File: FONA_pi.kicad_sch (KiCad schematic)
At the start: 31 parts, among them J1 Conn_01x20_Socket, J10 Conn_01x04_Pin, J11 Conn_01x20_Socket, J12 Conn_01x20_Socket, J13 Conn_01x06_Socket, J14 Conn_01x06_Socket, J15 Conn_01x06_Socket, J16 Conn_01x06_Socket, J17 Conn_01x06_Socket, J18 Conn_01x04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

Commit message: Placed footprints again.
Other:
- moved on the sheet: D2, D3

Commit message: Fixed DRC errors
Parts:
- renumbered JP1 to G5
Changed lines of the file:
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@@
   (symbol (lib_id "Jumper:Jumper_2_Bridged") (at 135.89 95.25 180) (unit 1)
     (in_bom yes) (on_board yes) (dnp no)
-    (property "Reference" "JP1" (at 135.89 92.71 0)
+    (property "Reference" "G5" (at 135.89 92.71 0)
       (effects (font (size 1.27 1.27)))
     )
@@
       (project "FONA_pi"
         (path "/78cf560b-fde9-4d4c-9c9c-e6052c5bcb78"
-          (reference "JP1") (unit 1)
+          (reference "G5") (unit 1)
         )
       )

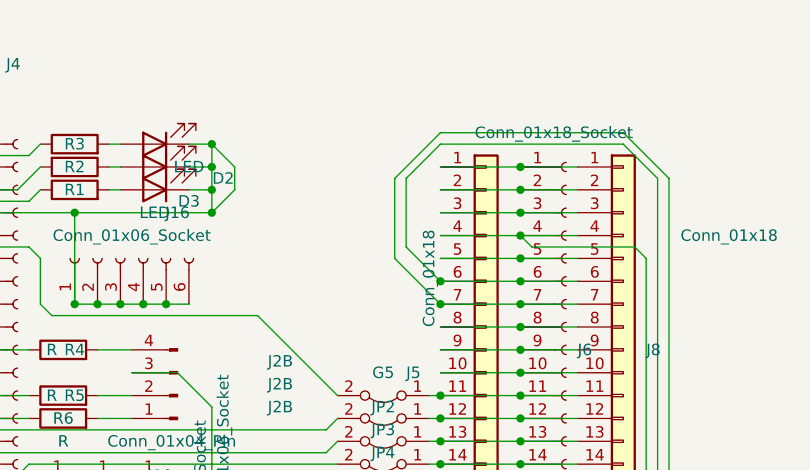
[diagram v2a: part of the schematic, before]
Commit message: Added connector pins J19 and J20, to associate with connectors in pcb.  Lost mounting holes
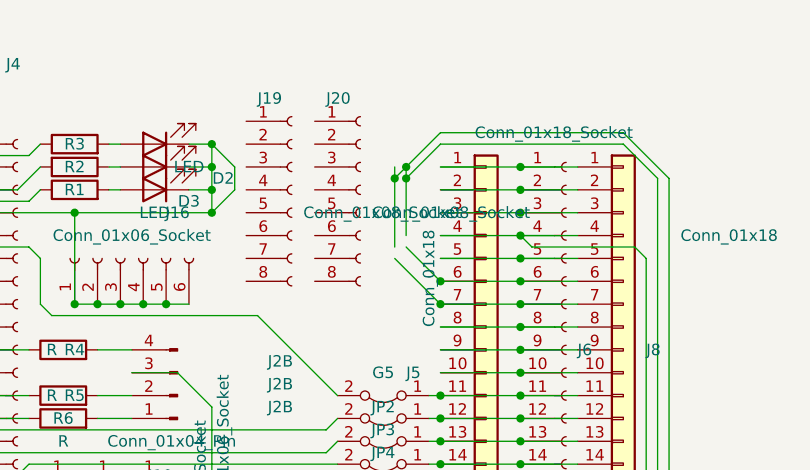
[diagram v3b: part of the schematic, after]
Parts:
- added J19, J20: Conn_01x08_Socket, Connector_PinSocket_2.54mm:PinSocket_1x08_P2.54mm_Vertical, symbol Connector:Conn_01x08_Socket
- J6: footprint Connector_PinSocket_2.54mm:PinSocket_1x18_P2.54mm_Vertical -> Connector_PinSocket_2.54mm:PinSocket_1x08_P2.54mm_Vertical
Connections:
- net at J2.10 (Pin_10), J3.16 (Pin_16), J4.16 (Pin_16)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: now also J2.8 (Pin_8), J3.17 (Pin_17), J4.17 (Pin_17), J7.17 (Pin_17); no longer J5.7 (Pin_7), J6.7 (Pin_7), J8.7 (Pin_7)
- new net: J5.6 (Pin_6), J6.6 (Pin_6), J8.6 (Pin_6)
- new net: J5.7 (Pin_7), J6.7 (Pin_7), J8.7 (Pin_7)
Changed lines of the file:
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@@
   (junction (at 102.87 106.68) (diameter 0) (color 0 0 0 0)
   )
+  (junction (at 138.43 71.12) (diameter 0) (color 0 0 0 0)
+  )
   (junction (at 83.82 77.47) (diameter 0) (color 0 0 0 0)
   )
@@
   (junction (at 54.61 95.25) (diameter 0) (color 0 0 0 0)
   )
+  (junction (at 138.43 69.85) (diameter 0) (color 0 0 0 0)
+  )
   (junction (at 44.45 110.49) (diameter 0) (color 0 0 0 0)
   )
@@
   (junction (at 151.13 107.95) (diameter 0) (color 0 0 0 0)
   )
+  (junction (at 137.16 71.12) (diameter 0) (color 0 0 0 0)
+  )
   (junction (at 45.72 97.79) (diameter 0) (color 0 0 0 0)
   )
@@
     (stroke (width 0) (type default))
   )
+  (wire (pts (xy 137.16 71.12) (xy 137.16 78.74))
+    (stroke (width 0) (type default))
+  )
   (wire (pts (xy 77.47 107.95) (xy 83.82 107.95))
     (stroke (width 0) (type default))
@@
     (stroke (width 0) (type default))
   )
-  (wire (pts (xy 137.16 71.12) (xy 142.24 66.04))
+  (wire (pts (xy 137.16 71.12) (xy 138.43 69.85))
     (stroke (width 0) (type default))
   )
@@
     (stroke (width 0) (type default))
   )
-  (wire (pts (xy 137.16 71.12) (xy 137.16 80.01))
+  (wire (pts (xy 138.43 71.12) (xy 138.43 77.47))
+    (stroke (width 0) (type default))
+  )
+  (wire (pts (xy 137.16 69.85) (xy 137.16 71.12))
     (stroke (width 0) (type default))
   )
@@
     (stroke (width 0) (type default))
   )
-  (wire (pts (xy 138.43 71.12) (xy 138.43 78.74))
+  (wire (pts (xy 138.43 69.85) (xy 138.43 71.12))
     (stroke (width 0) (type default))
   )
@@
   )
   (wire (pts (xy 113.03 92.71) (xy 116.84 96.52))
+    (stroke (width 0) (type default))
+  )
+  (wire (pts (xy 138.43 69.85) (xy 142.24 66.04))
     (stroke (width 0) (type default))
   )
@@
       (effects (font (size 1.27 1.27)) (justify left))
     )
-    (property "Footprint" "Connector_PinSocket_2.54mm:PinSocket_1x18_P2.54mm_Vertical" (at 156.21 90.17 0)
+    (property "Footprint" "Connector_PinSocket_2.54mm:PinSocket_1x08_P2.54mm_Vertical" (at 156.21 90.17 0)
       (effects (font (size 1.27 1.27)) hide)
     )
@@
     )
   )
+  (symbol (lib_id "Connector:Conn_01x08_Socket") (at 125.73 72.39 0) (unit 1)
+    (in_bom yes) (on_board yes) (dnp no)
+    (property "Reference" "J19" (at 121.92 62.23 0)
+      (effects (font (size 1.27 1.27)) (justify left))
+    )
+    (property "Value" "Conn_01x08_Socket" (at 127 74.93 0)
+      (effects (font (size 1.27 1.27)) (justify left))
+    )
+    (property "Footprint" "Connector_PinSocket_2.54mm:PinSocket_1x08_P2.54mm_Vertical" (at 125.73 72.39 0)
+      (effects (font (size 1.27 1.27)) hide)
+    )
+    (property "Datasheet" "~" (at 125.73 72.39 0)
+      (effects (font (size 1.27 1.27)) hide)
+    )
+    (pin "1")
+    (pin "2")
+    (pin "3")
+    (pin "4")
+    (pin "5")
+    (pin "6")
+    (pin "7")
+    (pin "8")
+    (instances
+      (project "FONA_pi"
+        (path "/78cf560b-fde9-4d4c-9c9c-e6052c5bcb78"
+          (reference "J19") (unit 1)
+        )
+      )
+    )
+  )
   (symbol (lib_id "Connector:Conn_01x20_Socket") (at 95.25 90.17 0) (unit 1)
     (in_bom yes) (on_board yes) (dnp no)
@@
         )
       )
+    )
+  )
+  (symbol (lib_id "Connector:Conn_01x08_Socket") (at 133.35 72.39 0) (unit 1)
+    (in_bom yes) (on_board yes) (dnp no)
+    (property "Reference" "J20" (at 129.54 62.23 0)
+      (effects (font (size 1.27 1.27)) (justify left))
+    )
+    (property "Value" "Conn_01x08_Socket" (at 134.62 74.93 0)
+      (effects (font (size 1.27 1.27)) (justify left))
+    )
+    (property "Footprint" "Connector_PinSocket_2.54mm:PinSocket_1x08_P2.54mm_Vertical" (at 133.35 72.39 0)
+      (effects (font (size 1.27 1.27)) hide)
+    )
+    (property "Datasheet" "~" (at 133.35 72.39 0)
+      (effects (font (size 1.27 1.27)) hide)
+    )
+    (pin "1")
+    (pin "2")
+    (pin "3")
+    (pin "4")
+    (pin "5")
+    (pin "6")
+    (pin "7")
+    (pin "8")
+    (instances
+      (project "FONA_pi"
+        (path "/78cf560b-fde9-4d4c-9c9c-e6052c5bcb78"
+          (reference "J20") (unit 1)
+        )
+      )

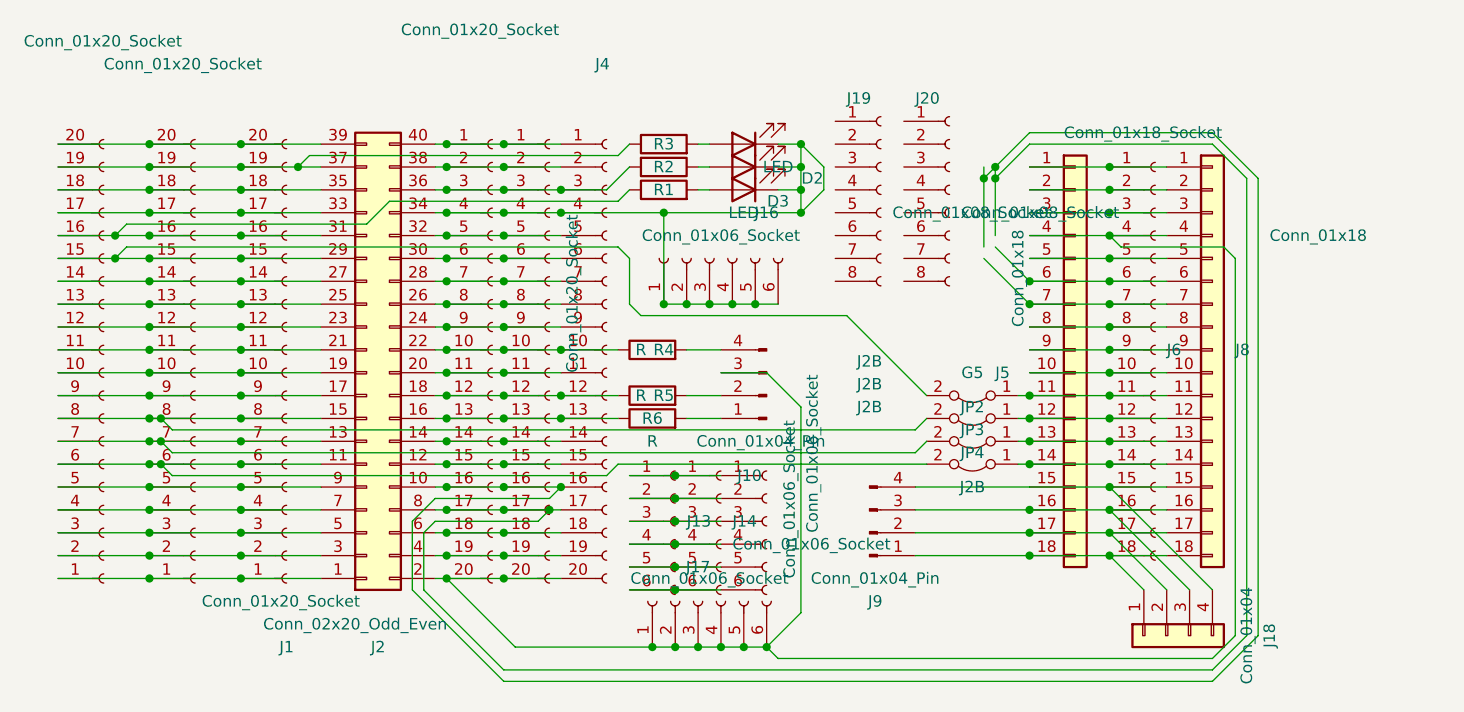
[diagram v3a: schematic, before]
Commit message: Reverted some changes.  Needs to update from schematic and see what breaks
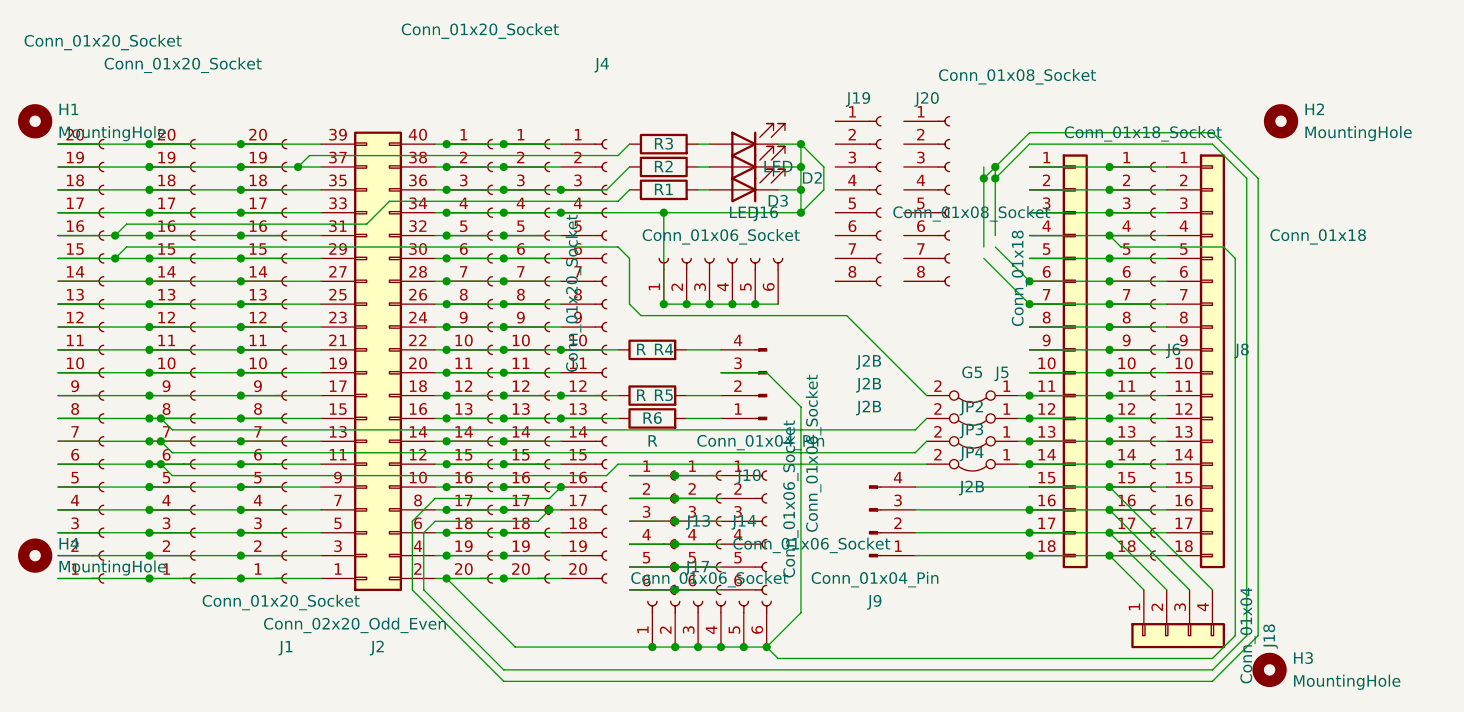
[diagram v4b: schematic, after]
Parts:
- added H1, H2, H3, H4: MountingHole, MountingHole:MountingHole_2.5mm, symbol Mechanical:MountingHole
- J6: footprint Connector_PinSocket_2.54mm:PinSocket_1x08_P2.54mm_Vertical -> Connector_PinHeader_2.54mm:PinHeader_1x18_P2.54mm_Vertical
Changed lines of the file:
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@@
+    )
+  )
+  (symbol (lib_id "Mechanical:MountingHole") (at 31.75 113.03 0) (unit 1)
+    (in_bom yes) (on_board yes) (dnp no) (fields_autoplaced)
+    (property "Reference" "H4" (at 34.29 111.76 0)
+      (effects (font (size 1.27 1.27)) (justify left))
+    )
+    (property "Value" "MountingHole" (at 34.29 114.3 0)
+      (effects (font (size 1.27 1.27)) (justify left))
+    )
+    (property "Footprint" "MountingHole:MountingHole_2.5mm" (at 31.75 113.03 0)
+      (effects (font (size 1.27 1.27)) hide)
+    )
+    (property "Datasheet" "~" (at 31.75 113.03 0)
+      (effects (font (size 1.27 1.27)) hide)
+    )
+    (instances
+      (project "FONA_pi"
+        (path "/78cf560b-fde9-4d4c-9c9c-e6052c5bcb78"
+          (reference "H4") (unit 1)
+        )
+      )
+    )
+  )
+  (symbol (lib_id "Mechanical:MountingHole") (at 168.91 125.73 0) (unit 1)
+    (in_bom yes) (on_board yes) (dnp no) (fields_autoplaced)
+    (property "Reference" "H3" (at 171.45 124.46 0)
+      (effects (font (size 1.27 1.27)) (justify left))
+    )
+    (property "Value" "MountingHole" (at 171.45 127 0)
+      (effects (font (size 1.27 1.27)) (justify left))
+    )
+    (property "Footprint" "MountingHole:MountingHole_2.5mm" (at 168.91 125.73 0)
+      (effects (font (size 1.27 1.27)) hide)
+    )
+    (property "Datasheet" "~" (at 168.91 125.73 0)
+      (effects (font (size 1.27 1.27)) hide)
+    )
+    (instances
+      (project "FONA_pi"
+        (path "/78cf560b-fde9-4d4c-9c9c-e6052c5bcb78"
+          (reference "H3") (unit 1)
+        )
+      )
+    )
+  )
+  (symbol (lib_id "Mechanical:MountingHole") (at 31.75 64.77 0) (unit 1)
+    (in_bom yes) (on_board yes) (dnp no) (fields_autoplaced)
+    (property "Reference" "H1" (at 34.29 63.5 0)
+      (effects (font (size 1.27 1.27)) (justify left))
+    )
+    (property "Value" "MountingHole" (at 34.29 66.04 0)
+      (effects (font (size 1.27 1.27)) (justify left))
+    )
+    (property "Footprint" "MountingHole:MountingHole_2.5mm" (at 31.75 64.77 0)
+      (effects (font (size 1.27 1.27)) hide)
+    )
+    (property "Datasheet" "~" (at 31.75 64.77 0)
+      (effects (font (size 1.27 1.27)) hide)
+    )
+    (instances
+      (project "FONA_pi"
+        (path "/78cf560b-fde9-4d4c-9c9c-e6052c5bcb78"
+          (reference "H1") (unit 1)
+        )
+      )
     )
   )
@@
       (effects (font (size 1.27 1.27)) (justify left))
     )
-    (property "Footprint" "Connector_PinSocket_2.54mm:PinSocket_1x08_P2.54mm_Vertical" (at 156.21 90.17 0)
+    (property "Footprint" "Connector_PinHeader_2.54mm:PinHeader_1x18_P2.54mm_Vertical" (at 156.21 90.17 0)
       (effects (font (size 1.27 1.27)) hide)
     )
@@
       (effects (font (size 1.27 1.27)) (justify left))
     )
-    (property "Value" "Conn_01x08_Socket" (at 134.62 74.93 0)
+    (property "Value" "Conn_01x08_Socket" (at 132.08 59.69 0)
       (effects (font (size 1.27 1.27)) (justify left))
     )
@@
         )
       )
+    )
+  )
+  (symbol (lib_id "Mechanical:MountingHole") (at 170.18 64.77 0) (unit 1)
+    (in_bom yes) (on_board yes) (dnp no) (fields_autoplaced)
+    (property "Reference" "H2" (at 172.72 63.5 0)
+      (effects (font (size 1.27 1.27)) (justify left))
+    )
+    (property "Value" "MountingHole" (at 172.72 66.04 0)
+      (effects (font (size 1.27 1.27)) (justify left))
+    )
+    (property "Footprint" "MountingHole:MountingHole_2.5mm" (at 170.18 64.77 0)
+      (effects (font (size 1.27 1.27)) hide)
+    )
+    (property "Datasheet" "~" (at 170.18 64.77 0)
+      (effects (font (size 1.27 1.27)) hide)
+    )
+    (instances
+      (project "FONA_pi"
+        (path "/78cf560b-fde9-4d4c-9c9c-e6052c5bcb78"
+          (reference "H2") (unit 1)
+        )
+      )

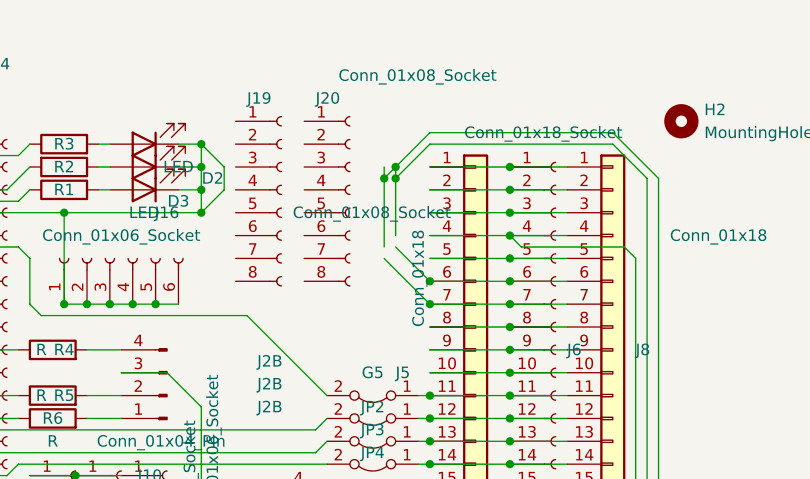
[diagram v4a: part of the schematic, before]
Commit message: Re-did some tracks after getting errors from updating from sch
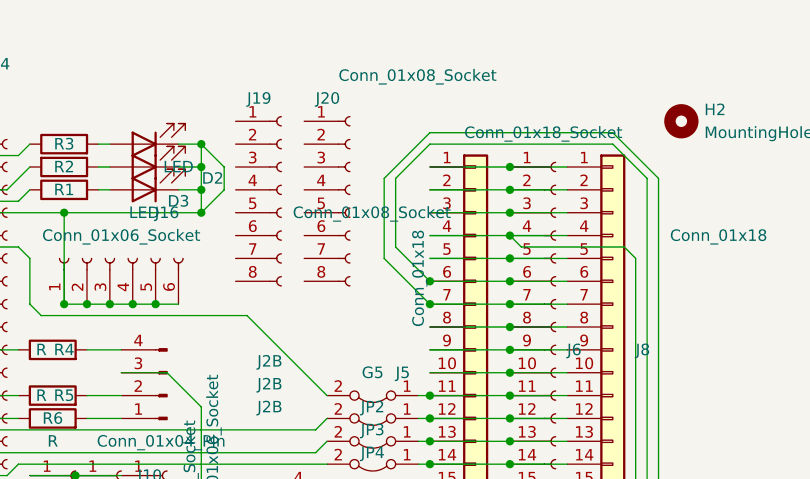
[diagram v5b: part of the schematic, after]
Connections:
- net at J2.10 (Pin_10), J3.16 (Pin_16), J4.16 (Pin_16)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: now also J5.7 (Pin_7), J6.7 (Pin_7), J8.7 (Pin_7); no longer J2.8 (Pin_8), J3.17 (Pin_17), J4.17 (Pin_17), J7.17 (Pin_17)
- net at J5.6 (Pin_6), J6.6 (Pin_6), J8.6 (Pin_6): now also J2.8 (Pin_8), J3.17 (Pin_17), J4.17 (Pin_17), J7.17 (Pin_17)
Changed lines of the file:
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@@
   (junction (at 102.87 106.68) (diameter 0) (color 0 0 0 0)
   )
-  (junction (at 138.43 71.12) (diameter 0) (color 0 0 0 0)
-  )
   (junction (at 83.82 77.47) (diameter 0) (color 0 0 0 0)
   )
@@
   (junction (at 54.61 95.25) (diameter 0) (color 0 0 0 0)
   )
-  (junction (at 138.43 69.85) (diameter 0) (color 0 0 0 0)
-  )
   (junction (at 44.45 110.49) (diameter 0) (color 0 0 0 0)
   )
@@
   (junction (at 151.13 107.95) (diameter 0) (color 0 0 0 0)
   )
-  (junction (at 137.16 71.12) (diameter 0) (color 0 0 0 0)
-  )
   (junction (at 45.72 97.79) (diameter 0) (color 0 0 0 0)
   )
@@
     (stroke (width 0) (type default))
   )
+  (wire (pts (xy 142.24 67.31) (xy 138.43 71.12))
+    (stroke (width 0) (type default))
+  )
   (wire (pts (xy 83.82 97.79) (xy 90.17 97.79))
     (stroke (width 0) (type default))
@@
     (stroke (width 0) (type default))
   )
-  (wire (pts (xy 137.16 71.12) (xy 137.16 78.74))
-    (stroke (width 0) (type default))
-  )
   (wire (pts (xy 77.47 107.95) (xy 83.82 107.95))
     (stroke (width 0) (type default))
@@
     (stroke (width 0) (type default))
   )
-  (wire (pts (xy 137.16 71.12) (xy 138.43 69.85))
-    (stroke (width 0) (type default))
-  )
   (wire (pts (xy 116.84 69.85) (xy 116.84 72.39))
     (stroke (width 0) (type default))
@@
     (stroke (width 0) (type default))
   )
-  (wire (pts (xy 138.43 71.12) (xy 138.43 77.47))
-    (stroke (width 0) (type default))
-  )
-  (wire (pts (xy 137.16 69.85) (xy 137.16 71.12))
-    (stroke (width 0) (type default))
-  )
   (wire (pts (xy 44.45 69.85) (xy 54.61 69.85))
     (stroke (width 0) (type default))
@@
     (stroke (width 0) (type default))
   )
-  (wire (pts (xy 142.24 67.31) (xy 138.43 71.12))
-    (stroke (width 0) (type default))
-  )
   (wire (pts (xy 142.24 82.55) (xy 151.13 82.55))
     (stroke (width 0) (type default))
@@
     (stroke (width 0) (type default))
   )
-  (wire (pts (xy 138.43 69.85) (xy 138.43 71.12))
+  (wire (pts (xy 138.43 71.12) (xy 138.43 78.74))
     (stroke (width 0) (type default))
   )
@@
     (stroke (width 0) (type default))
   )
-  (wire (pts (xy 138.43 69.85) (xy 142.24 66.04))
+  (wire (pts (xy 137.16 71.12) (xy 142.24 66.04))
     (stroke (width 0) (type default))
   )
@@
     (stroke (width 0) (type default))
   )
+  (wire (pts (xy 137.16 71.12) (xy 137.16 80.01))
+    (stroke (width 0) (type default))
+  )
